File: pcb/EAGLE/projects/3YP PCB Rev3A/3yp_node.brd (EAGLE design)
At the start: 104.3 x 24.4 mm, 51 parts, among them IC1 ATSAMR30M18A-I_RM100, IC2 TPS78233DDCT, IC3 DS3231SN#, IC4 AT25DF321A-SH-B, J1 19-46-1-TGG, J2 M20-9980445, J3 M20-9990445, J4 M20-9990445, J5 M20-9990445, J6 M20-9990445, U1 1042P

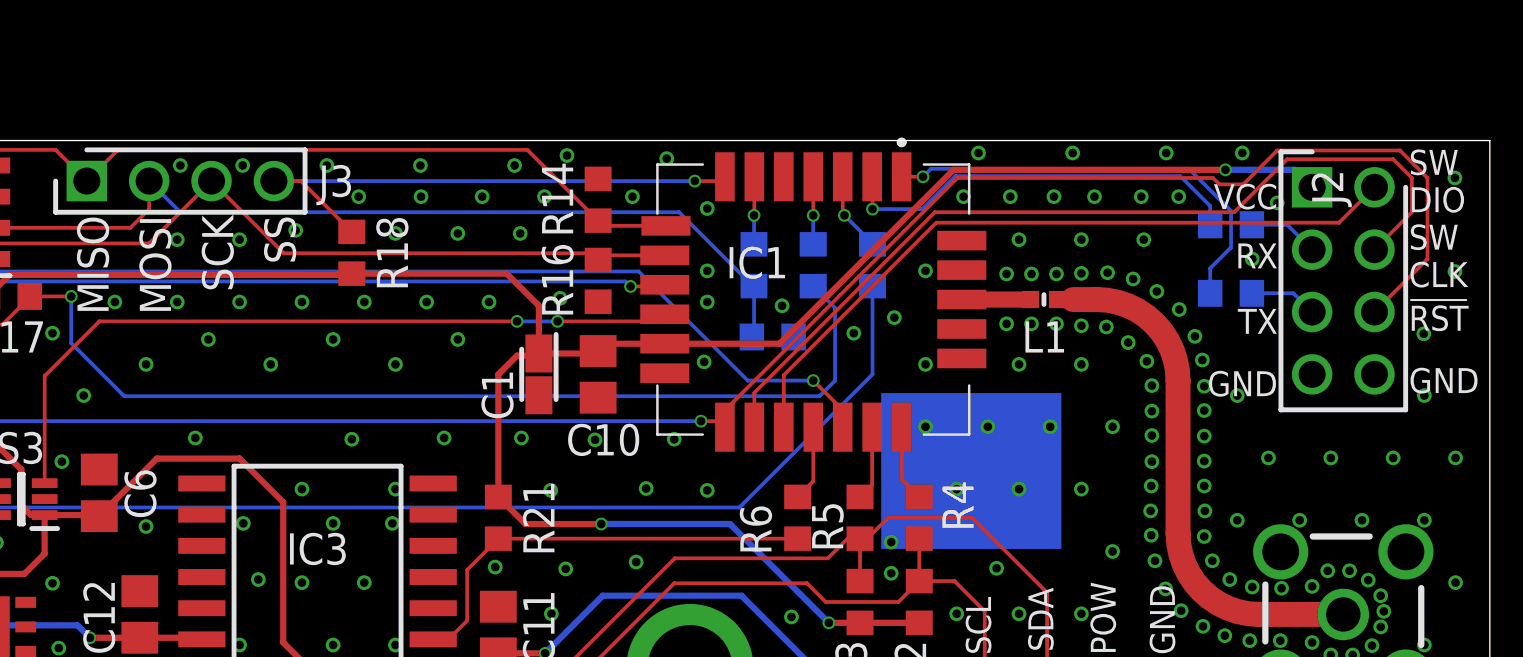
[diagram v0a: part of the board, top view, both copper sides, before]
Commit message: Finished node layout and added programmer PCB
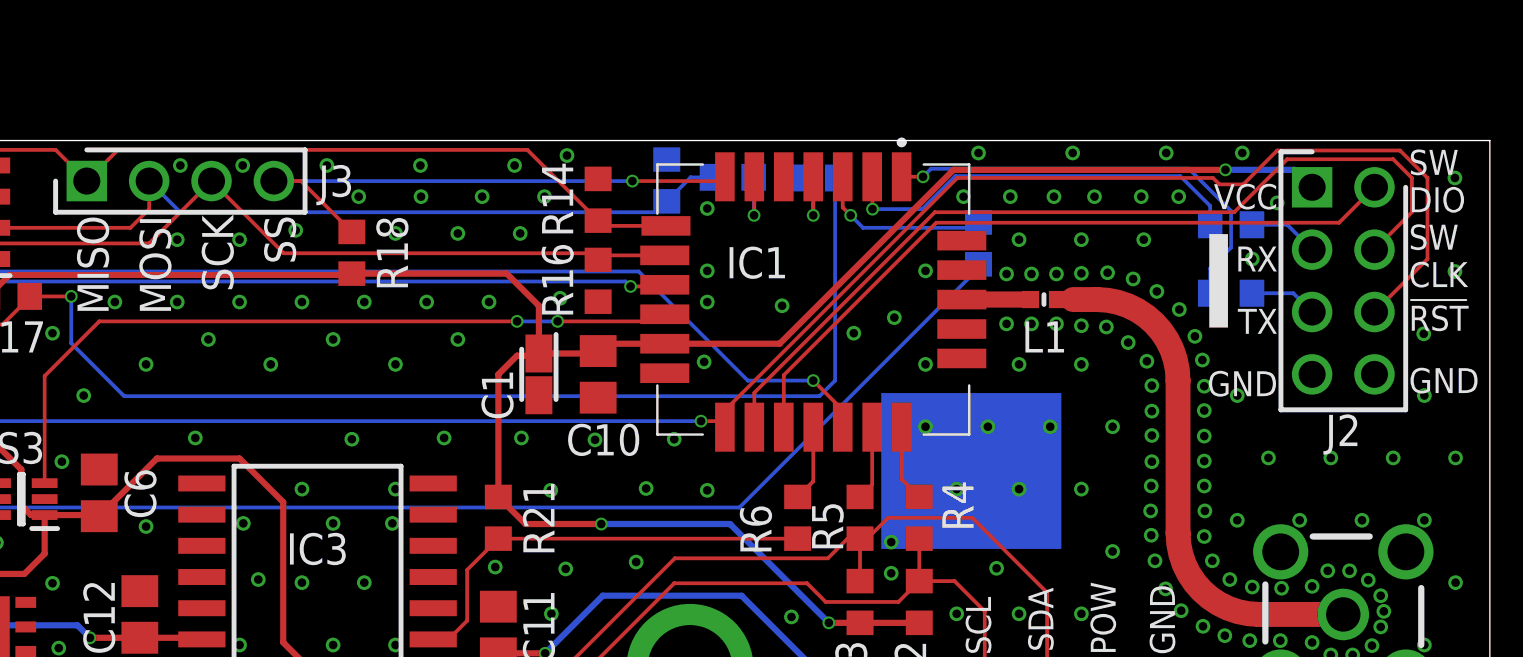
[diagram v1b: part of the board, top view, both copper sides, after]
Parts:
- moved R15 7.70 mm to (70.7, 22.8), turned to 90 degrees
- moved R2 4.41 mm to (83.4, 20.2)
- moved R3 3.68 mm to (73.4, 22.9), turned to 0 degrees
- moved R1 3.56 mm to (76.8, 22.9), turned to 180 degrees
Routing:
- net PA16_SPI_MISO: track 36.5 -> 32.0 mm
- net !PA15_SPI_FLASH_SS: track 48.8 -> 52.8 mm
- net N$4: track 3.26 -> 7.21 mm
- net PA14_USRLED: track 57.5 -> 60.2 mm
- net N$2: track 2.75 -> 3.39 mm
